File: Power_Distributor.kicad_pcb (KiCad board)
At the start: 2 copper layers, 200 x 100 mm, 139 parts, among them J1 Thruster_Off_Switch, P1 XT60, P10 XT60, P11 XT60, P12 XT60, P13 XT60, P14 XT60, P15 XT60, P16 XT60, P17 XT60, P18 XT60, P19 USB_B, P2 XT60, P20 XT60, P21 XT60, P22 XT60, P23 XT60, P24 XT60, P25 XT60, P26 XT60, P27 XT60, P28 XT60, P29 XT60, P3 XT60, P4 XT60, P5 XT60, P6 XT60, P7 XT60, P8 XT60, P9 XT60, Q10 IPD90P03P4L, Q12 IPD90P03P4L, Q13 AUIRFS8409-7P, Q14 AUIRFS8409-7P, Q15 BC817-40, Q2 IPD90P03P4L, Q4 IPD90P03P4L, Q6 IPD90P03P4L, Q8 IPD90P03P4L, U1 93LC56BT-I/OT, U10 TEN_20-2411WIN, U11 TEN_20-2411WIN, U2 FT232H, U3 ACPL-247-500E, U4 ACPL-247-500E, U5 LTC4357, U6 LTC4357, U7 UWE-12/6-Q12P, U8 UWE-12/6-Q12P, U9 UWE-12/6-Q12P, Y1 12MHz

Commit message: Update Netlist
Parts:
- removed C20, C21, C22, C23, C24: 100nF, Capacitors_SMD:C_0603
- removed D18, D19, D20, D21: Led_Small, LEDs:LED_0603
- removed Q10, Q12: IPD90P03P4L, TO_SOT_Packages_SMD:TO-252-2Lead
- removed Q13, Q14: AUIRFS8409-7P, Zeabus:D2PAK-7
- removed Q15: BC817-40, TO_SOT_Packages_SMD:SOT-23
- removed R40, R41, R42, R43: 150, Resistors_SMD:R_0603
- removed R44, R45: 10k, Resistors_SMD:R_0603
- removed R46, R47, R48, R51, R52: 1k, Resistors_SMD:R_0603
- removed U11: TEN_20-2411WIN, Zeabus:TEN_20WIN
- added C1, C2, C4, C5: 100nF, Capacitors_SMD:C_0603, F.Cu at (145.0, 155.1)
- added C3, C6: 4.7uF, Capacitors_SMD:C_0805, F.Cu at (145.0, 155.1)
- added D11: BZX585-C12, Diodes_SMD:D_SOD-523, F.Cu at (145.0, 155.1)
- added D14: Led_Small, LEDs:LED_0603, F.Cu at (145.0, 155.1)
- added D8: LED_Small, LEDs:LED_0603, F.Cu at (145.0, 155.1)
- added Q1, Q3, Q5: IPD90P03P4L, TO_SOT_Packages_SMD:TO-252-2Lead, F.Cu at (145.0, 155.1)
- added Q7: AUIRFS8409-7P, Zeabus:D2PAK-7, F.Cu at (145.0, 155.1)
- added Q9: BC817-40, TO_SOT_Packages_SMD:SOT-23, F.Cu at (145.0, 155.1)
- added R11, R17, R2: 1k, Resistors_SMD:R_0603, F.Cu at (145.0, 155.1)
- added R12, R16, R21, R22, R6, R7: 10k, Resistors_SMD:R_0603, F.Cu at (145.0, 155.1)
- added R26, R27: 150, Resistors_SMD:R_0603, F.Cu at (145.0, 155.1)
- C11, C7: value 100nF -> 27pF
- C13: value 27pF -> 4.7uF; footprint Capacitors_SMD:C_0603 -> Capacitors_SMD:C_0805
- C17: value 27pF -> 100nF
- C18, C9: value 4.7uF -> 100nF; footprint Capacitors_SMD:C_0805 -> Capacitors_SMD:C_0603
- C19: value 4.7uF -> 100uF; footprint Capacitors_SMD:C_0805 -> Capacitors_SMD:CP_Elec_8x10.5
- D12, D2, D4, D6: value BZX585-C12 -> LED_Small; footprint Diodes_SMD:D_SOD-523 -> LEDs:LED_0603
- D13, D16: value LED_Small -> Led_Small
- D3, D5, D7: value LED_Small -> BZX585-C12; footprint LEDs:LED_0603 -> Diodes_SMD:D_SOD-523
- Q8: value IPD90P03P4L -> AUIRFS8409-7P; footprint TO_SOT_Packages_SMD:TO-252-2Lead -> Zeabus:D2PAK-7
- R19, R4, R9: value 1k -> 10k
- R20: value 10k -> 2.2k
- R24: value 1k -> 12k 1%
- R25, R28, R30, R31: value 10k -> 150
- R29: value 1k -> 150
- R32: value 2.2k -> 10k
- R33, R34, R5, R8: value 10k -> 1k
- R36: value 12k 1% -> 10k
- R37: value 150 -> 1.4k
- R38, R39: value 150 -> 1k
- U10: value TEN_20-2411WIN -> I6A24014A033V; footprint Zeabus:TEN_20WIN -> zeabus:I6A24014A033V
- U8, U9: value UWE-12/6-Q12P -> TEN_20-2411WIN; footprint Zeabus:UWE-xxxx -> Zeabus:TEN_20WIN
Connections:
- C10 pad 1: VBUS -> GND
- C10 pad 2: GND -> Net-(C10-Pad2)
- C12 pad 1: +3V3 -> Net-(C12-Pad1)
- C14 pad 1: +3V3 -> Net-(C12-Pad1)
- C15 pad 1: GND -> Net-(C13-Pad1)
- C15 pad 2: Net-(C15-Pad2) -> GND
- C16 pad 1: GND -> +3V3
- C16 pad 2: Net-(C16-Pad2) -> GND
- C17 pad 1: Net-(C17-Pad1) -> +3V3
- C18 pad 1: Net-(C18-Pad1) -> +3V3
- C19 pad 1: Net-(C19-Pad1) -> +BATT
- C7 pad 1: +3V3 -> Net-(C7-Pad1)
- C8 pad 1: Net-(C8-Pad1) -> +3V3
- C9 pad 1: VBUS -> GND
- C9 pad 2: GND -> Net-(C9-Pad2)
- D1 pad 1: /DC-DC Converter/Lamp_SW_C -> +BATT
- D1 pad 2: GND -> Net-(D1-Pad2)
- D12 pad 1: +BATT -> GND
- D13 pad 1: GND -> Net-(D13-Pad1)
- D15 pad 1: +BATT -> /DC-DC Converter/Lamp_SW_C
- D15 pad 2: Net-(D15-Pad2) -> GND
- D16 pad 1: GND -> Net-(D16-Pad1)
- D2 pad 1: +BATT -> GND
- D3 pad 1: GND -> +BATT
- D4 pad 1: +BATT -> GND
- D5 pad 1: GND -> +BATT
- D6 pad 1: +BATT -> GND
- D7 pad 1: GND -> +BATT
- L1 pad 1: Net-(C8-Pad1) -> Net-(C2-Pad1)
- L2 pad 2: Net-(C18-Pad1) -> Net-(C12-Pad1)
- L3 pad 2: Net-(C19-Pad1) -> Net-(C13-Pad1)
- P19 pad 1: Net-(C8-Pad1) -> Net-(C2-Pad1)
- P22 pad 2: Net-(D17-Pad1) -> Net-(D13-Pad1)
- P23 pad 2: Net-(D18-Pad1) -> Net-(D14-Pad1)
- P24 pad 1: Net-(P24-Pad1) -> Net-(P22-Pad1)
- P24 pad 2: Net-(D19-Pad1) -> Net-(D13-Pad1)
- P25 pad 2: Net-(D17-Pad1) -> Net-(D13-Pad1)
- P26 pad 1: Net-(P22-Pad1) -> Net-(P23-Pad1)
- P26 pad 2: Net-(D17-Pad1) -> Net-(D14-Pad1)
- P27 pad 2: Net-(D20-Pad1) -> Net-(D16-Pad1)
- P28 pad 2: Net-(D21-Pad1) -> Net-(D17-Pad1)
- P29 pad 1: Net-(P27-Pad1) -> Net-(P28-Pad1)
- P29 pad 2: Net-(D20-Pad1) -> Net-(D17-Pad1)
- Q2 pad 1: Net-(D2-Pad2) -> Net-(D3-Pad2)
- Q2 pad 2: Net-(F1-Pad1) -> +BATT
- Q2 pad 3: +BATT -> Net-(F2-Pad1)
- Q4 pad 1: Net-(D4-Pad2) -> Net-(D7-Pad2)
- Q4 pad 2: +BATT -> Net-(F4-Pad1)
- Q4 pad 3: Net-(F2-Pad1) -> +BATT
- Q6 pad 1: Net-(D6-Pad2) -> Net-(D11-Pad2)
- Q6 pad 2: +BATT -> Net-(F6-Pad1)
- Q6 pad 3: Net-(F3-Pad1) -> +BATT
- R1 pad 1: /DC-DC Converter/Lamp_SW_C -> +BATT
- R1 pad 2: +BATT -> /Power_Controller/SW2_C
- R10 pad 1: Net-(D5-Pad2) -> +BATT
- R10 pad 2: Net-(F2-Pad2) -> /Power_Controller/SW5_C
- R13 pad 2: /Power_Controller/SW4_C -> /Power_Controller/SW6_C
- R14 pad 1: Net-(D6-Pad2) -> Net-(D9-Pad2)
- R14 pad 2: /Power_Controller/SW4_C -> /Power_Controller/SW6_C
- R15 pad 1: Net-(D7-Pad2) -> Net-(F5-Pad2)
- R15 pad 2: Net-(F3-Pad2) -> Net-(D10-Pad2)
- R18 pad 1: +BATT -> Net-(F6-Pad2)
- R18 pad 2: /Power_Controller/SW5_C -> Net-(D12-Pad2)
- R19 pad 1: Net-(D9-Pad2) -> Net-(R19-Pad1)
- R19 pad 2: /Power_Controller/SW5_C -> +3V3
- R20 pad 1: Net-(F4-Pad2) -> Net-(R20-Pad1)
- R20 pad 2: Net-(D10-Pad2) -> Net-(R20-Pad2)
- R23 pad 1: +BATT -> Net-(C5-Pad1)
- R23 pad 2: /Power_Controller/SW6_C -> +3V3
- R24 pad 1: Net-(D12-Pad2) -> GND
- R24 pad 2: /Power_Controller/SW6_C -> Net-(R24-Pad2)
- R25 pad 1: Net-(F5-Pad2) -> Net-(R25-Pad1)
- R25 pad 2: Net-(D13-Pad2) -> Net-(R25-Pad2)
- R28 pad 1: +BATT -> Net-(R28-Pad1)
- R28 pad 2: /Power_Controller/SW1_C -> Net-(R28-Pad2)
- R29 pad 1: Net-(D15-Pad2) -> Net-(R29-Pad1)
- R29 pad 2: /Power_Controller/SW1_C -> Net-(R29-Pad2)
- R3 pad 1: +BATT -> Net-(F1-Pad2)
- R3 pad 2: /Power_Controller/SW2_C -> Net-(D2-Pad2)
- R30 pad 1: Net-(F6-Pad2) -> Net-(R30-Pad1)
- R30 pad 2: Net-(D16-Pad2) -> Net-(R30-Pad2)
- R31 pad 2: +3V3 -> Net-(R31-Pad2)
- R32 pad 1: Net-(R32-Pad1) -> Net-(JP1-Pad2)
- R32 pad 2: Net-(R32-Pad2) -> +BATT
- R33 pad 1: Net-(R33-Pad1) -> Net-(D13-Pad2)
- R33 pad 2: +3V3 -> Net-(P22-Pad1)
- R34 pad 1: Net-(R32-Pad2) -> Net-(D14-Pad2)
- R34 pad 2: +3V3 -> Net-(P23-Pad1)
- R35 pad 1: Net-(C11-Pad1) -> /DC-DC Converter/Lamp_SW_C
- R35 pad 2: +3V3 -> +BATT
- R36 pad 1: GND -> /DC-DC Converter/Lamp_SW_E
- R36 pad 2: Net-(R36-Pad2) -> GND
- R37 pad 2: Net-(R37-Pad2) -> Net-(D17-Pad1)
- R38 pad 1: Net-(R38-Pad1) -> Net-(D16-Pad2)
- R38 pad 2: Net-(R38-Pad2) -> Net-(P27-Pad1)
- R39 pad 1: Net-(R39-Pad1) -> Net-(D17-Pad2)
- R39 pad 2: Net-(R39-Pad2) -> Net-(P28-Pad1)
- R4 pad 1: Net-(D2-Pad2) -> +BATT
- R4 pad 2: /Power_Controller/SW2_C -> /Power_Controller/SW3_C
- R5 pad 1: Net-(F1-Pad2) -> Net-(D3-Pad2)
- R5 pad 2: Net-(D3-Pad2) -> /Power_Controller/SW3_C
- R8 pad 1: +BATT -> Net-(D5-Pad2)
- R8 pad 2: /Power_Controller/SW3_C -> /Power_Controller/SW4_C
- R9 pad 1: Net-(D4-Pad2) -> Net-(D6-Pad2)
- R9 pad 2: /Power_Controller/SW3_C -> Net-(F3-Pad2)
- U1 pad 1: Net-(R32-Pad1) -> Net-(R20-Pad1)
- U1 pad 3: Net-(R32-Pad2) -> Net-(R20-Pad2)
- U1 pad 4: Net-(R33-Pad1) -> Net-(R21-Pad1)
- U1 pad 5: Net-(R31-Pad1) -> Net-(R19-Pad1)
- U10 pad 2: GND -> /DC-DC Converter/Lamp_SW_E
- U10 pad 3: Net-(P27-Pad1) -> GND
- U10 pad 4: Net-(U10-Pad4) -> Net-(D17-Pad1)
- U10 pad 6: Net-(Q15-Pad3) -> Net-(R37-Pad1)
- U2 pad 1: Net-(C13-Pad1) -> Net-(C7-Pad1)
- U2 pad 2: Net-(C17-Pad1) -> Net-(C11-Pad1)
- U2 pad 21: Net-(R37-Pad1) -> Net-(R25-Pad1)
- U2 pad 25: Net-(R38-Pad1) -> Net-(R26-Pad1)
- U2 pad 27: Net-(R39-Pad1) -> Net-(R27-Pad1)
- U2 pad 28: Net-(R40-Pad1) -> Net-(R28-Pad1)
- U2 pad 29: Net-(R41-Pad1) -> Net-(R29-Pad1)
- U2 pad 3: Net-(C19-Pad1) -> Net-(C13-Pad1)
- U2 pad 30: Net-(R42-Pad1) -> Net-(R30-Pad1)
- U2 pad 31: Net-(R43-Pad1) -> Net-(R31-Pad1)
- U2 pad 34: Net-(C11-Pad1) -> Net-(C5-Pad1)
- U2 pad 37: Net-(C16-Pad2) -> Net-(C10-Pad2)
- U2 pad 38: Net-(C15-Pad2) -> Net-(C9-Pad2)
- U2 pad 43: Net-(R32-Pad2) -> Net-(R20-Pad2)
- U2 pad 44: Net-(R33-Pad1) -> Net-(R21-Pad1)
- U2 pad 45: Net-(R31-Pad1) -> Net-(R19-Pad1)
- U2 pad 5: Net-(R36-Pad2) -> Net-(R24-Pad2)
- U2 pad 8: Net-(C18-Pad1) -> Net-(C12-Pad1)
- U3 pad 1: Net-(R37-Pad2) -> Net-(R25-Pad2)
- U3 pad 3: Net-(R38-Pad2) -> Net-(R26-Pad2)
- U3 pad 7: Net-(R39-Pad2) -> Net-(R27-Pad2)
- U4 pad 1: Net-(R40-Pad2) -> Net-(R28-Pad2)
- U4 pad 3: Net-(R41-Pad2) -> Net-(R29-Pad2)
- U4 pad 5: Net-(R42-Pad2) -> Net-(R30-Pad2)
- U4 pad 7: Net-(R43-Pad2) -> Net-(R31-Pad2)
- U6 pad 4: Net-(Q14-PadG) -> Net-(Q8-PadG)
- U7 pad 2: Net-(Q15-Pad3) -> Net-(Q9-Pad3)
- U7 pad 4: Net-(D17-Pad1) -> Net-(D13-Pad1)
- U8 pad 2: /DC-DC Converter/Lamp_SW_E -> GND
- U8 pad 3: GND -> Net-(P23-Pad1)
- U8 pad 4: Net-(D18-Pad1) -> Net-(U8-Pad4)
- U8 pad 5: Net-(U8-Pad5) -> Net-(D14-Pad1)
- U8 pad 6: Net-(U8-Pad6) -> Net-(Q9-Pad3)
- U9 pad 2: /DC-DC Converter/Lamp_SW_E -> GND
- U9 pad 3: GND -> Net-(P27-Pad1)
- U9 pad 4: Net-(D19-Pad1) -> Net-(U9-Pad4)
- U9 pad 5: Net-(U9-Pad5) -> Net-(D16-Pad1)
- U9 pad 6: Net-(U9-Pad6) -> /DC-DC Converter/DSP_Switch_C
- Y1 pad 1: Net-(C13-Pad1) -> Net-(C7-Pad1)
- Y1 pad 2: Net-(C17-Pad1) -> Net-(C11-Pad1)

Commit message: Ver1 Power_dist PCB
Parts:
- removed D10: LED_Small, LEDs:LED_0603
- removed D9: BZX585-C12, Diodes_SMD:D_SOD-523
- removed F5: Fuse, zeabus:FUSE_AUTO
- removed P11, P12, P13, P14: XT60, zeabus:XT60
- removed Q5: IPD90P03P4L, TO_SOT_Packages_SMD:TO-252-2Lead
- removed R13, R15: 10k, Resistors_SMD:R_0603
- removed R14: 1k, Resistors_SMD:R_0603
- added REF**: 1pin, Connectors:1pin, F.Cu at (80.5, 47.9)
- added REF**: 1pin, Connectors:1pin, F.Cu at (222.0, 48.3)
- added REF**: 1pin, Connectors:1pin, F.Cu at (241.8, 141.7)
- added REF**: 1pin, Connectors:1pin, F.Cu at (82.3, 139.6)
- C10, C13, C15, C5, L3, R23, R24, R28, R29, R30, R31, U4: moved to B.Cu
- moved U8 322.3 mm to (227.7, 128.3), turned to 90 degrees
- moved U9 319.4 mm to (201.0, 128.3), turned to 90 degrees
- moved P26 227.7 mm to (227.9, 79.2), turned to 180 degrees
- moved U10 223.6 mm to (128.7, 133.3), turned to 180 degrees
- moved D7 217.6 mm to (82.5, 60.5), turned to 180 degrees
- moved Q6 206.3 mm to (72.4, 56.7), turned to 90 degrees
- moved P23 205.2 mm to (227.9, 88.1), turned to 180 degrees
- moved P28 201.3 mm to (120.4, 138.3)
- moved R37 197.9 mm to (94.6, 115.6), turned to 90 degrees
- moved P27 196.4 mm to (200.9, 87.8), turned to 180 degrees
- moved U7 196.3 mm to (162.1, 64.0)
- moved R39 193.4 mm to (93.2, 137.6), turned to 90 degrees
- moved D17 185.3 mm to (93.0, 140.8), turned to 90 degrees
- moved C19 183.4 mm to (137.9, 129.0), turned to 270 degrees
- moved R36 181.5 mm to (131.7, 137.3), turned to 90 degrees
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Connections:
- Q2 pad 2: +BATT -> Net-(F2-Pad1)
- Q2 pad 3: Net-(F2-Pad1) -> +BATT
- Q3 pad 2: +BATT -> Net-(F3-Pad1)
- Q3 pad 3: Net-(F3-Pad1) -> +BATT
- U4 pad 13: /Kill_SW -> /Power_Controller/SW6_E
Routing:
- net Net-(Q9-Pad3): track 0.00 -> 435.8 mm, vias 0 -> 1
- net /Power_Controller/SW1_C: track 0.00 -> 377.2 mm
- net /Power_Controller/SW2_C: track 0.00 -> 328.9 mm
- net +BATT: track 0.00 -> 281.0 mm
- net /Power_Controller/SW3_C: track 0.00 -> 227.9 mm
- net GND: track 0.00 -> 221.8 mm, vias 0 -> 14
- net /DC-DC Converter/Lamp_SW_E: track 0.00 -> 204.2 mm, vias 0 -> 2
- net /Power_Controller/SW5_C: track 0.00 -> 184.0 mm, vias 0 -> 1
- net /DC-DC Converter/Lamp_SW_C: track 0.00 -> 178.1 mm, vias 0 -> 1
- net Net-(P22-Pad1): track 0.00 -> 145.8 mm
- net /Power_Controller/SW4_C: track 0.00 -> 144.8 mm
- net /DC-DC Converter/DSP_Switch_C: track 0.00 -> 139.0 mm
- net Net-(D13-Pad1): track 0.00 -> 86.6 mm
- net Net-(D17-Pad1): track 0.00 -> 85.9 mm
- net +3V3: track 0.00 -> 85.1 mm, vias 0 -> 4
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- added copper zone on F.Cu, net +BATT
- added copper zone on B.Cu, net GND
- added copper zone on F.Cu, net Net-(F1-Pad1)
- added copper zone on F.Cu, net Net-(F1-Pad2)
- added copper zone on F.Cu, net Net-(F2-Pad1)
- added copper zone on F.Cu, net Net-(F2-Pad2)
- added copper zone on F.Cu, net Net-(F3-Pad1)
- added copper zone on F.Cu, net Net-(F3-Pad2)
- added copper zone on F.Cu, net Net-(F4-Pad1)
- added copper zone on F.Cu, net Net-(F4-Pad2)
- added copper zone on F.Cu, net Net-(F6-Pad1)
- added copper zone on F.Cu, net Net-(F6-Pad2)
- added copper zone on F.Cu, net Net-(F7-Pad1)
- added copper zone on F.Cu, net Net-(F7-Pad2)
- added copper zone on F.Cu, net Net-(F8-Pad1)
- added copper zone on F.Cu, net Net-(F8-Pad2)

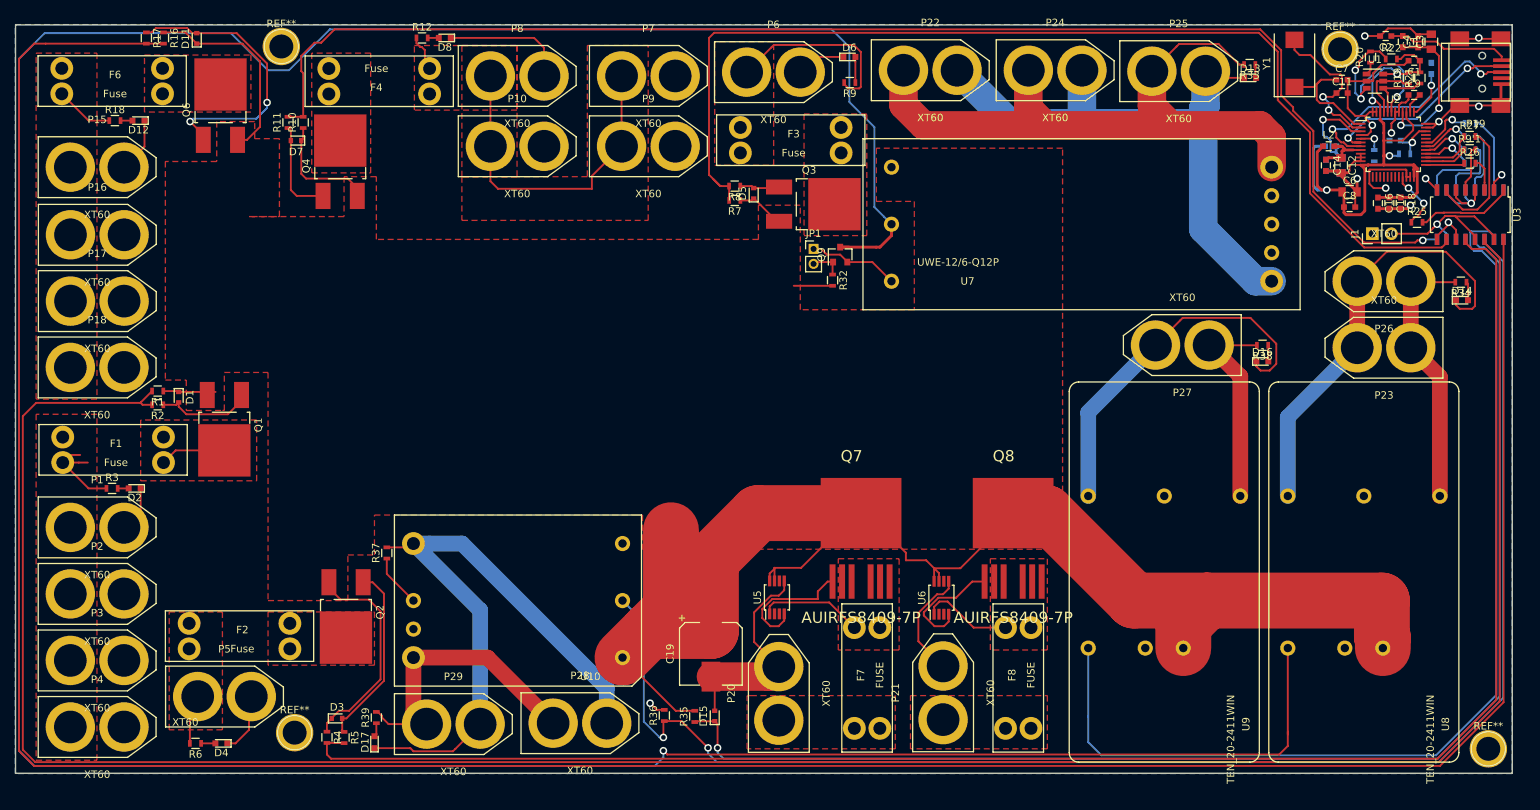
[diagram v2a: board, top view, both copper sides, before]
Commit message: Correct GND mixed-up and re-route USB signals as a differential pairs with match length.
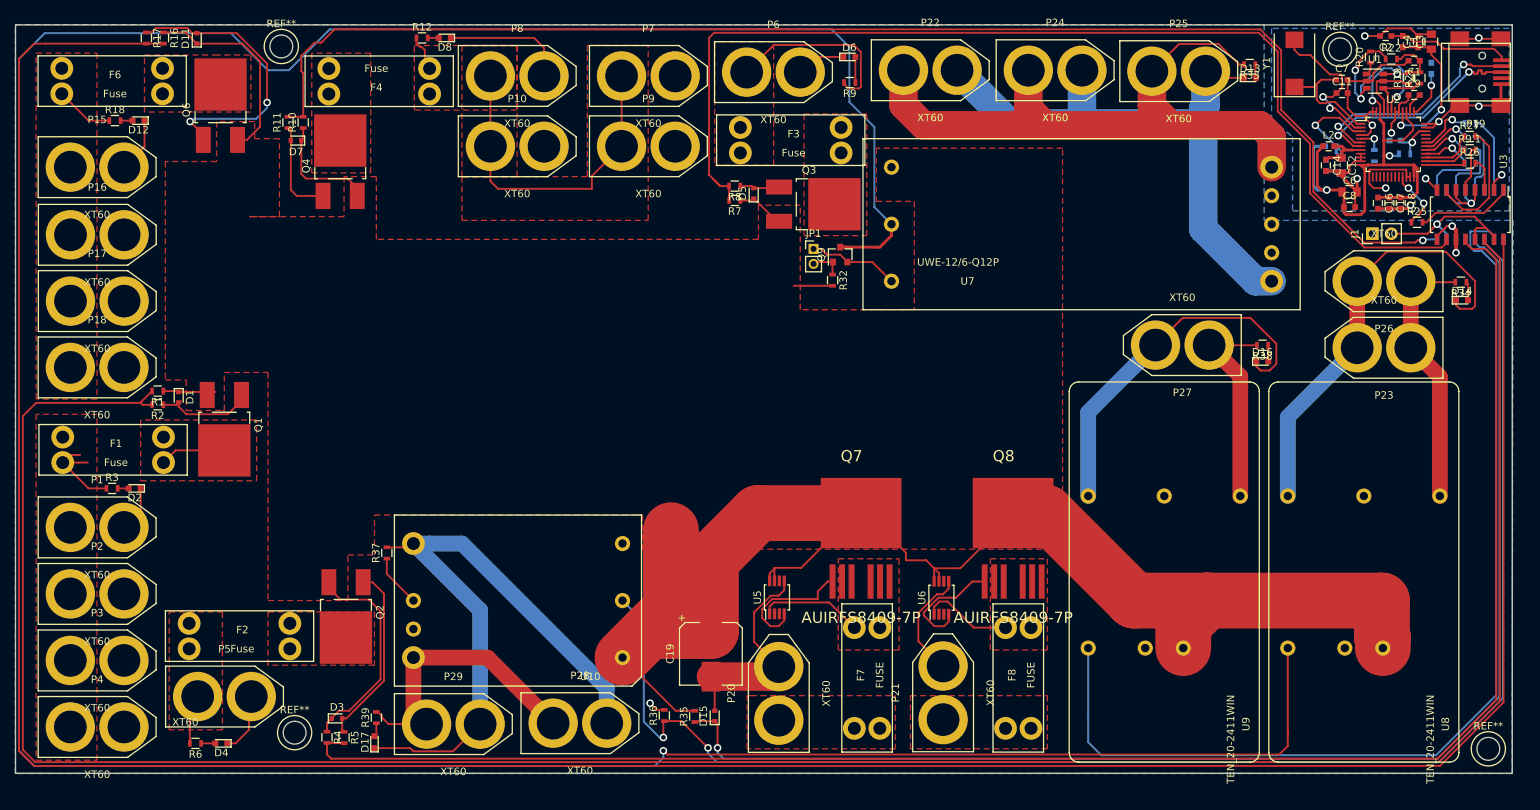
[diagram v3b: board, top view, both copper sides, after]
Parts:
- U10: footprint zeabus:I6A24014A033V -> Zeabus:I6A24014A033V
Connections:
- net Net-(P19-Pad2) renamed /Power_Controller/D-
- net Net-(P19-Pad3) renamed /Power_Controller/D+
- C1 pad 2: GND -> GNDD
- C10 pad 1: GND -> GNDD
- C11 pad 2: GND -> GNDD
- C12 pad 2: GND -> GNDD
- C13 pad 2: GND -> GNDD
- C14 pad 2: GND -> GNDD
- C15 pad 2: GND -> GNDD
- C16 pad 2: GND -> GNDD
- C17 pad 2: GND -> GNDD
- C18 pad 2: GND -> GNDD
- C2 pad 2: GND -> GNDD
- C3 pad 2: GND -> GNDD
- C4 pad 2: GND -> GNDD
- C5 pad 2: GND -> GNDD
- C6 pad 2: GND -> GNDD
- C7 pad 2: GND -> GNDD
- C8 pad 2: GND -> GNDD
- C9 pad 1: GND -> GNDD
- P19 pad 5: GND -> GNDD
- P19 pad 6: GND -> GNDD
- R24 pad 1: GND -> GNDD
- U1 pad 2: GND -> GNDD
- U2 pad 10: GND -> GNDD
- U2 pad 11: GND -> GNDD
- U2 pad 22: GND -> GNDD
- U2 pad 23: GND -> GNDD
- U2 pad 35: GND -> GNDD
- U2 pad 36: GND -> GNDD
- U2 pad 4: GND -> GNDD
- U2 pad 41: GND -> GNDD
- U2 pad 42: GND -> GNDD
- U2 pad 47: GND -> GNDD
- U2 pad 48: GND -> GNDD
- U2 pad 9: GND -> GNDD
- U3 pad 2: GND -> GNDD
- U3 pad 4: GND -> GNDD
- U3 pad 6: GND -> GNDD
- U3 pad 8: GND -> GNDD
- U4 pad 2: GND -> GNDD
- U4 pad 4: GND -> GNDD
- U4 pad 6: GND -> GNDD
- U4 pad 8: GND -> GNDD
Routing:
- net GNDD: track 0.00 -> 110.6 mm, vias 0 -> 12
- net GND: track 221.8 -> 115.1 mm, vias 14 -> 3
- net /Power_Controller/D-: track 27.3 -> 29.9 mm
- net /Power_Controller/D+: track 32.4 -> 29.9 mm
- net /Kill_SW: track 23.5 -> 22.0 mm
- net Net-(C13-Pad1): track 16.3 -> 17.0 mm
- net VBUS: track 20.2 -> 20.7 mm
- added copper zone on B.Cu, net GNDD

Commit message: Debug , Edit Mounting Hole size , Ref val position
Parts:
- REF** (x4): footprint Connectors:1pin -> Mounting_Holes:MountingHole_3.2mm_M3
- moved R20 0.74 mm to (226.6, 48.8)
- moved REF** 0.72 mm to (242.3, 142.2)
- moved F3 0.65 mm to (154.7, 62.0)
- moved REF** 0.57 mm to (222.2, 47.8)
- moved REF** 0.46 mm to (80.8, 47.5)
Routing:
- net Net-(R20-Pad2): track 27.1 -> 29.3 mm
- net Net-(R20-Pad1): track 1.73 -> 2.54 mm
- net /Power_Controller/SW5_C: track 184.0 -> 183.5 mm
- net GNDD: track 110.6 -> 110.0 mm
- net Net-(Q9-Pad3): track 435.8 -> 436.3 mm

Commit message: Bug fixed
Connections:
- R22 pad 1: Net-(R20-Pad2) -> Net-(R20-Pad1)
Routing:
- net Net-(R20-Pad2): track 29.3 -> 22.1 mm
- net +3V3: track 85.1 -> 83.0 mm
- net Net-(R20-Pad1): track 2.54 -> 4.14 mm
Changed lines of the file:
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@@
     (links 297)
     (no_connects 0)
-    (area 44.924999 41.642419 246.7232 147.5182)
+    (area 44.924999 44.924999 245.075001 145.075001)
     (thickness 1.6)
     (drawings 4)
-    (tracks 1049)
+    (tracks 1042)
     (zones 0)
     (modules 131)
@@
     (fp_line (start 1.25 0.7) (end -1.25 0.7) (layer F.CrtYd) (width 0.05))
     (pad 1 smd rect (at -0.75 0) (size 0.5 0.9) (layers F.Cu F.Paste F.Mask)
-      (net 89 "Net-(R20-Pad2)"))
+      (net 88 "Net-(R20-Pad1)"))
     (pad 2 smd rect (at 0.75 0) (size 0.5 0.9) (layers F.Cu F.Paste F.Mask)
       (net 1 +3V3))
@@
   (gr_line (start 245 145) (end 245 45) (layer Edge.Cuts) (width 0.15))
   (gr_line (start 45 145) (end 245 145) (layer Edge.Cuts) (width 0.15))
+  (segment (start 229.616 51.816) (end 229.616 51.562) (width 0.254) (layer B.Cu) (net 1))
+  (segment (start 226.314 55.118) (end 229.616 51.816) (width 0.254) (layer B.Cu) (net 1))
   (segment (start 220.218 67.056) (end 219.49958 67.056) (width 0.381) (layer F.Cu) (net 1))
   (segment (start 218.948 66.50442) (end 218.948 61.976) (width 0.381) (layer F.Cu) (net 1))
@@
   (segment (start 229.616 51.562) (end 227.752 51.562) (width 0.254) (layer F.Cu) (net 1))
   (via (at 229.616 51.562) (size 1.016) (drill 0.6096) (layers F.Cu B.Cu) (net 1))
-  (segment (start 228.854 50.8) (end 229.616 51.562) (width 0.254) (layer B.Cu) (net 1))
-  (segment (start 227.838 50.8) (end 228.854 50.8) (width 0.254) (layer B.Cu) (net 1))
-  (segment (start 226.314 52.324) (end 227.838 50.8) (width 0.254) (layer B.Cu) (net 1))
-  (segment (start 226.314 55.118) (end 226.314 52.324) (width 0.254) (layer B.Cu) (net 1))
   (via (at 226.314 55.118) (size 1.016) (drill 0.6096) (layers F.Cu B.Cu) (net 1))
   (segment (start 226.77 55.118) (end 226.314 55.118) (width 0.254) (layer F.Cu) (net 1))
@@
   (segment (start 226.891799 52.588201) (end 226.968 52.512) (width 0.254) (layer F.Cu) (net 87))
   (segment (start 226.968 52.512) (end 227.752 52.512) (width 0.254) (layer F.Cu) (net 87))
-  (segment (start 226.568 50.650046) (end 226.568 49.506) (width 0.254) (layer F.Cu) (net 88))
-  (segment (start 225.552 51.562) (end 225.656046 51.562) (width 0.254) (layer F.Cu) (net 88))
-  (segment (start 225.656046 51.562) (end 226.568 50.650046) (width 0.254) (layer F.Cu) (net 88))
-  (segment (start 228.092 49.554) (end 228.092 48.006) (width 0.254) (layer F.Cu) (net 89))
-  (segment (start 224.79 54.864) (end 224.79 51.308) (width 0.254) (layer B.Cu) (net 89))
-  (segment (start 224.79 51.308) (end 228.092 48.006) (width 0.254) (layer B.Cu) (net 89))
-  (segment (start 226.822 48.768) (end 226.568 48.514) (width 0.254) (layer F.Cu) (net 89))
-  (segment (start 226.568 48.514) (end 226.568 48.006) (width 0.254) (layer F.Cu) (net 89))
-  (segment (start 227.506 48.768) (end 226.822 48.768) (width 0.254) (layer F.Cu) (net 89))
-  (segment (start 228.092 49.354) (end 227.506 48.768) (width 0.254) (layer F.Cu) (net 89))
+  (segment (start 226.568 49.506) (end 226.368 49.506) (width 0.254) (layer F.Cu) (net 88))
+  (segment (start 226.368 49.506) (end 225.552 50.322) (width 0.254) (layer F.Cu) (net 88))
+  (segment (start 225.552 50.322) (end 225.552 50.983) (width 0.254) (layer F.Cu) (net 88))
+  (segment (start 225.552 50.983) (end 225.552 51.562) (width 0.254) (layer F.Cu) (net 88))
+  (segment (start 228.092 49.554) (end 226.616 49.554) (width 0.254) (layer F.Cu) (net 88))
+  (segment (start 226.616 49.554) (end 226.568 49.506) (width 0.254) (layer F.Cu) (net 88))
+  (segment (start 224.282 54.864) (end 224.282 54.732) (width 0.254) (layer F.Cu) (net 89))
+  (segment (start 224.282 54.732) (end 225.552 53.462) (width 0.254) (layer F.Cu) (net 89))
+  (segment (start 228.092 48.006) (end 228.092 51.054) (width 0.254) (layer B.Cu) (net 89))
+  (via (at 224.282 54.864) (size 1.016) (drill 0.6096) (layers F.Cu B.Cu) (net 89))
+  (segment (start 228.092 51.054) (end 224.282 54.864) (width 0.254) (layer B.Cu) (net 89))
+  (segment (start 228.092 48.006) (end 226.568 48.006) (width 0.254) (layer F.Cu) (net 89))
+  (segment (start 229.637328 50.34279) (end 229.637328 49.551328) (width 0.254) (layer B.Cu) (net 89))
+  (segment (start 229.637328 49.551328) (end 228.092 48.006) (width 0.254) (layer B.Cu) (net 89))
+  (via (at 228.092 48.006) (size 1.016) (drill 0.6096) (layers F.Cu B.Cu) (net 89))
   (segment (start 229.616 54.61) (end 230.454201 53.771799) (width 0.254) (layer B.Cu) (net 89))
-  (segment (start 224.79 53.201408) (end 224.79 54.14558) (width 0.254) (layer B.Cu) (net 89))
   (segment (start 230.454201 53.771799) (end 230.454201 51.159663) (width 0.254) (layer B.Cu) (net 89))
   (segment (start 230.454201 51.159663) (end 229.637328 50.34279) (width 0.254) (layer B.Cu) (net 89))
-  (segment (start 229.637328 50.34279) (end 227.648618 50.34279) (width 0.254) (layer B.Cu) (net 89))
-  (segment (start 227.648618 50.34279) (end 224.79 53.201408) (width 0.254) (layer B.Cu) (net 89))
-  (segment (start 224.79 54.14558) (end 224.79 54.864) (width 0.254) (layer B.Cu) (net 89))
-  (segment (start 224.79 54.864) (end 224.79 54.224) (width 0.254) (layer F.Cu) (net 89))
-  (segment (start 224.79 54.224) (end 225.552 53.462) (width 0.254) (layer F.Cu) (net 89))
-  (via (at 224.79 54.864) (size 1.016) (drill 0.6096) (layers F.Cu B.Cu) (net 89))
   (segment (start 228.858 56.61) (end 228.858 55.368) (width 0.254) (layer F.Cu) (net 89))
   (segment (start 228.858 55.368) (end 229.616 54.61) (width 0.254) (layer F.Cu) (net 89))
   (via (at 229.616 54.61) (size 1.016) (drill 0.6096) (layers F.Cu B.Cu) (net 89))
-  (segment (start 228.092 49.354) (end 228.092 49.554) (width 0.254) (layer F.Cu) (net 89))
-  (via (at 228.092 48.006) (size 1.016) (drill 0.6096) (layers F.Cu B.Cu) (net 89))
-  (segment (start 228.092 49.784) (end 228.092 49.554) (width 0.254) (layer F.Cu) (net 89))
   (segment (start 232.664 52.832) (end 232.464 52.832) (width 0.254) (layer F.Cu) (net 90))
   (segment (start 232.464 52.832) (end 231.834 53.462) (width 0.254) (layer F.Cu) (net 90))
